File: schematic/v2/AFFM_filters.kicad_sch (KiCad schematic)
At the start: 24 parts, among them K1 DIPxx-1Axx-11x, K2 DIPxx-1Axx-11x, K3 DIPxx-1Axx-11x, K4 DIPxx-1Axx-11x

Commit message: dip switch symbol. how might this work...
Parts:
- added SW1: SW_DIP_x04, symbol Switch:SW_DIP_x04
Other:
- moved on the sheet: C12, C13, C15, C16, C17, D34, D35, D36, K2, K3, K4, R60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

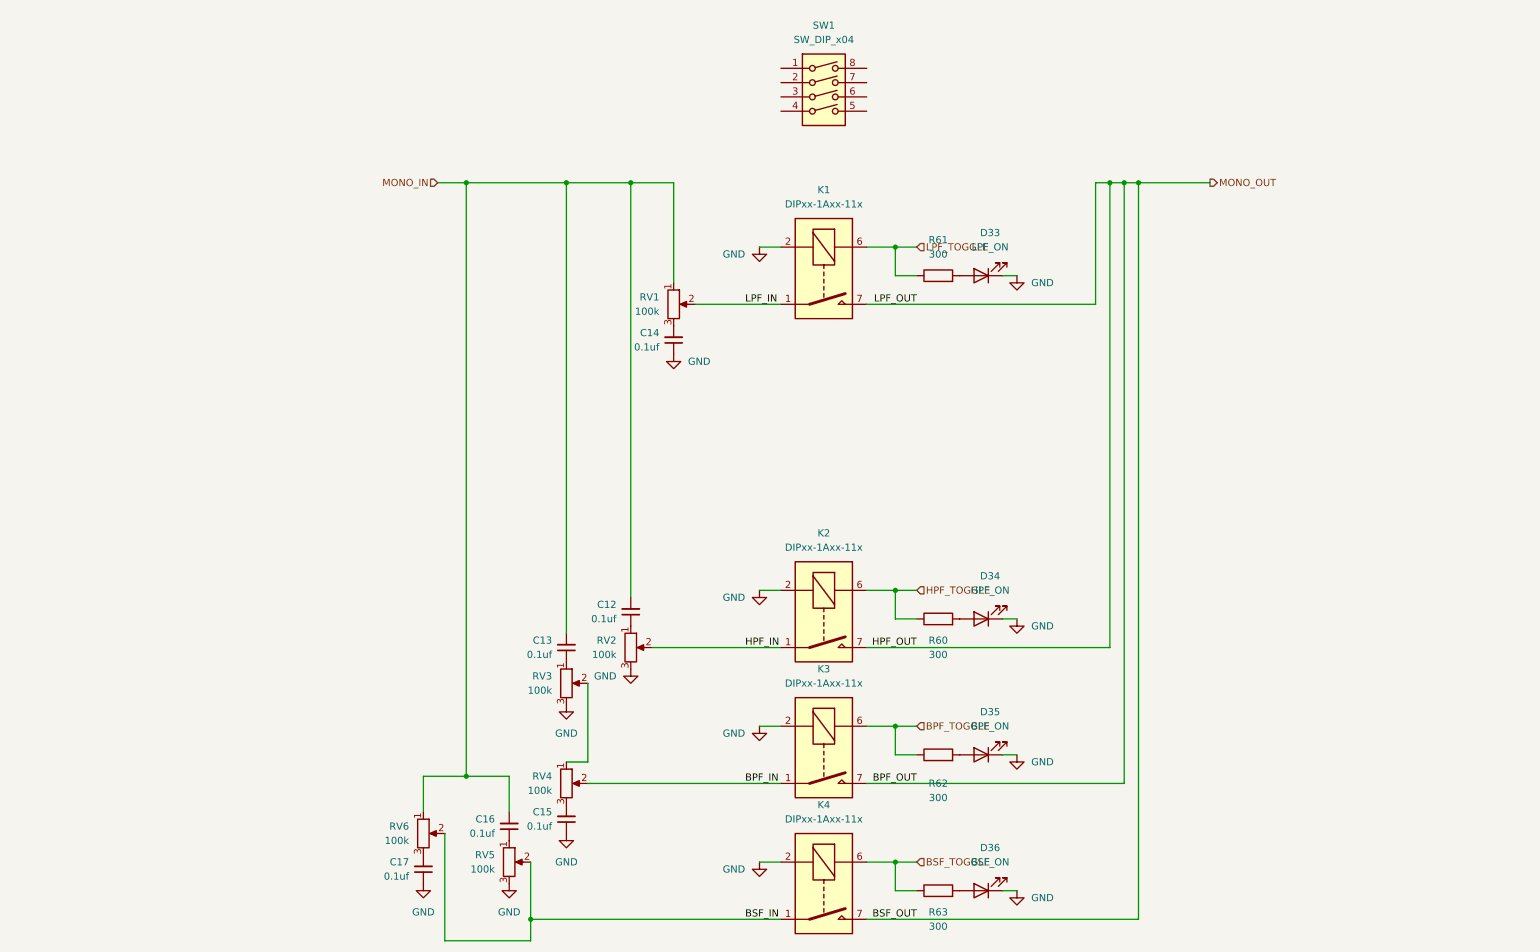
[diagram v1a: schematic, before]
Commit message: cool LPFs. i want to add some toggleability between my RC passive and active implementations...
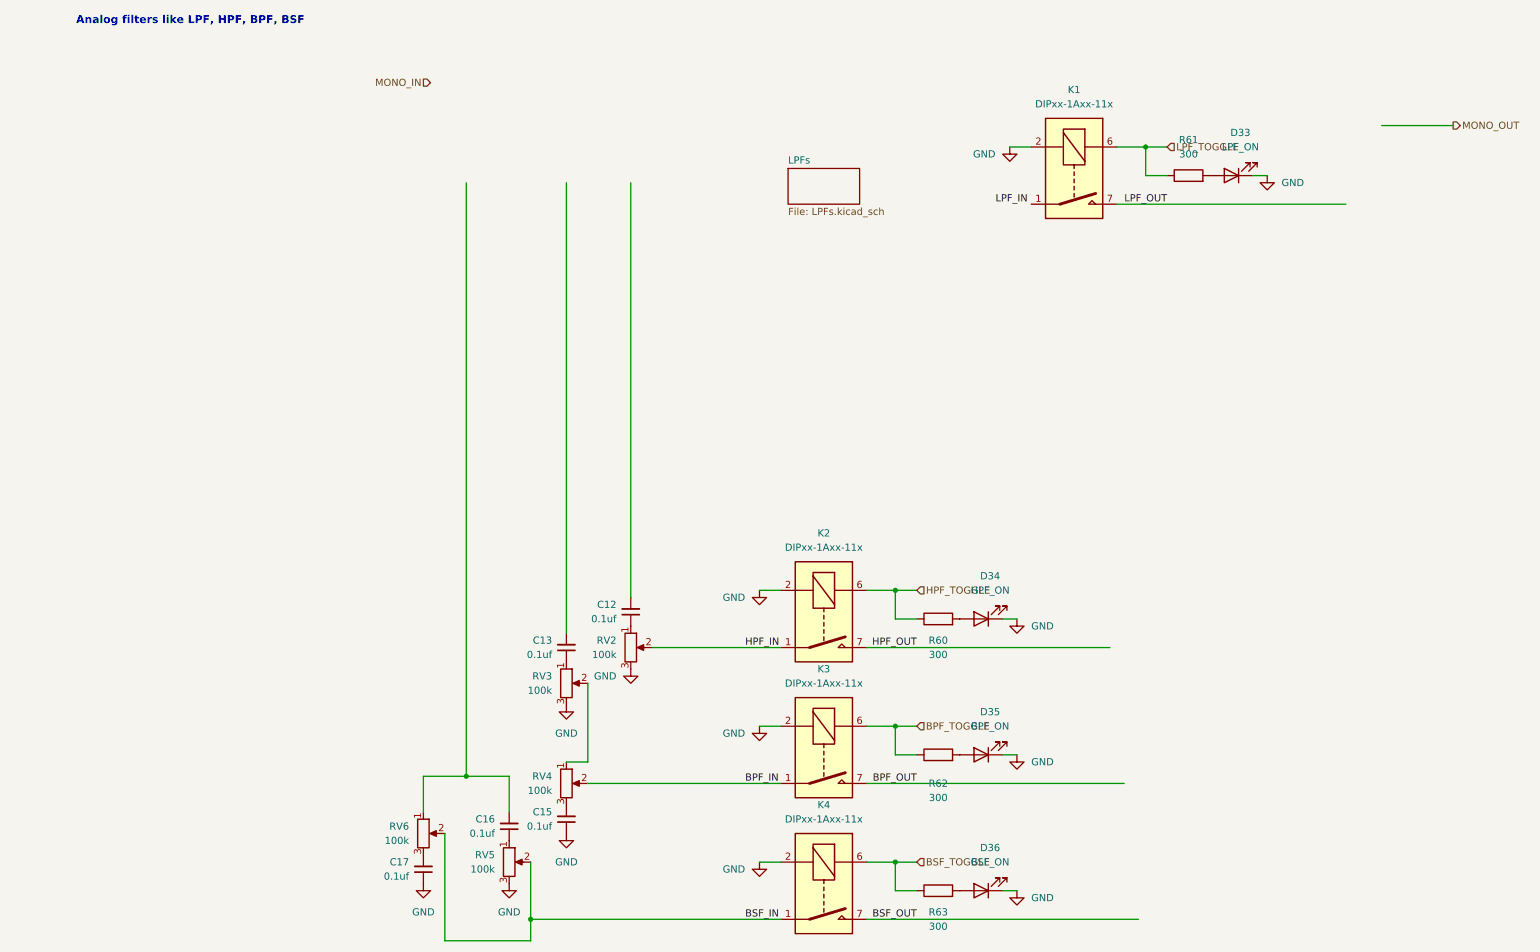
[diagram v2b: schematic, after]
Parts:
- removed C14: 0.1uf, Capacitor_SMD:C_0805_2012Metric, symbol Device:C_Small
- removed RV1: 100k, Potentiometer_THT:Potentiometer_Alps_RK09Y11_Single_Horizontal, symbol Device:R_Potentiometer
- removed SW1: SW_DIP_x04, symbol Switch:SW_DIP_x04
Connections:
- net LPF_IN: no longer K1.1, K1.14
- net MONO_IN: no longer C12.2, C13.2, C16.2, RV6.1
- net MONO_OUT: no longer K1.7, K1.8, K2.7, K2.8, K3.7, K3.8, K4.7, K4.8
- new net: C16.2, RV6.1
- new net: K1.1, K1.14
- new net BPF_OUT: K3.7, K3.8
- new net BSF_OUT: K4.7, K4.8
- new net HPF_OUT: K2.7, K2.8
- new net LPF_OUT: K1.7, K1.8
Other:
- added sheet LPFs (LPFs.kicad_sch)
- note added: "Analog filters like LPF, HPF, BPF, BSF"
- moved on the sheet: D33, K1, R61

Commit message: some progress on affm board
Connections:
- net LPF_OUT is gone; now on net MONO_OUT: K1.7, K1.8
- net LPF_IN: now also K1.1, K1.14
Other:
- sheet LPFs ports: added 12V+, 12V-, LPF_MONO_OUT, MONO_IN; removed none
- moved on the sheet: C12, C13, C15, C16, C17, D34, D35, D36, K2, K3, K4, R60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

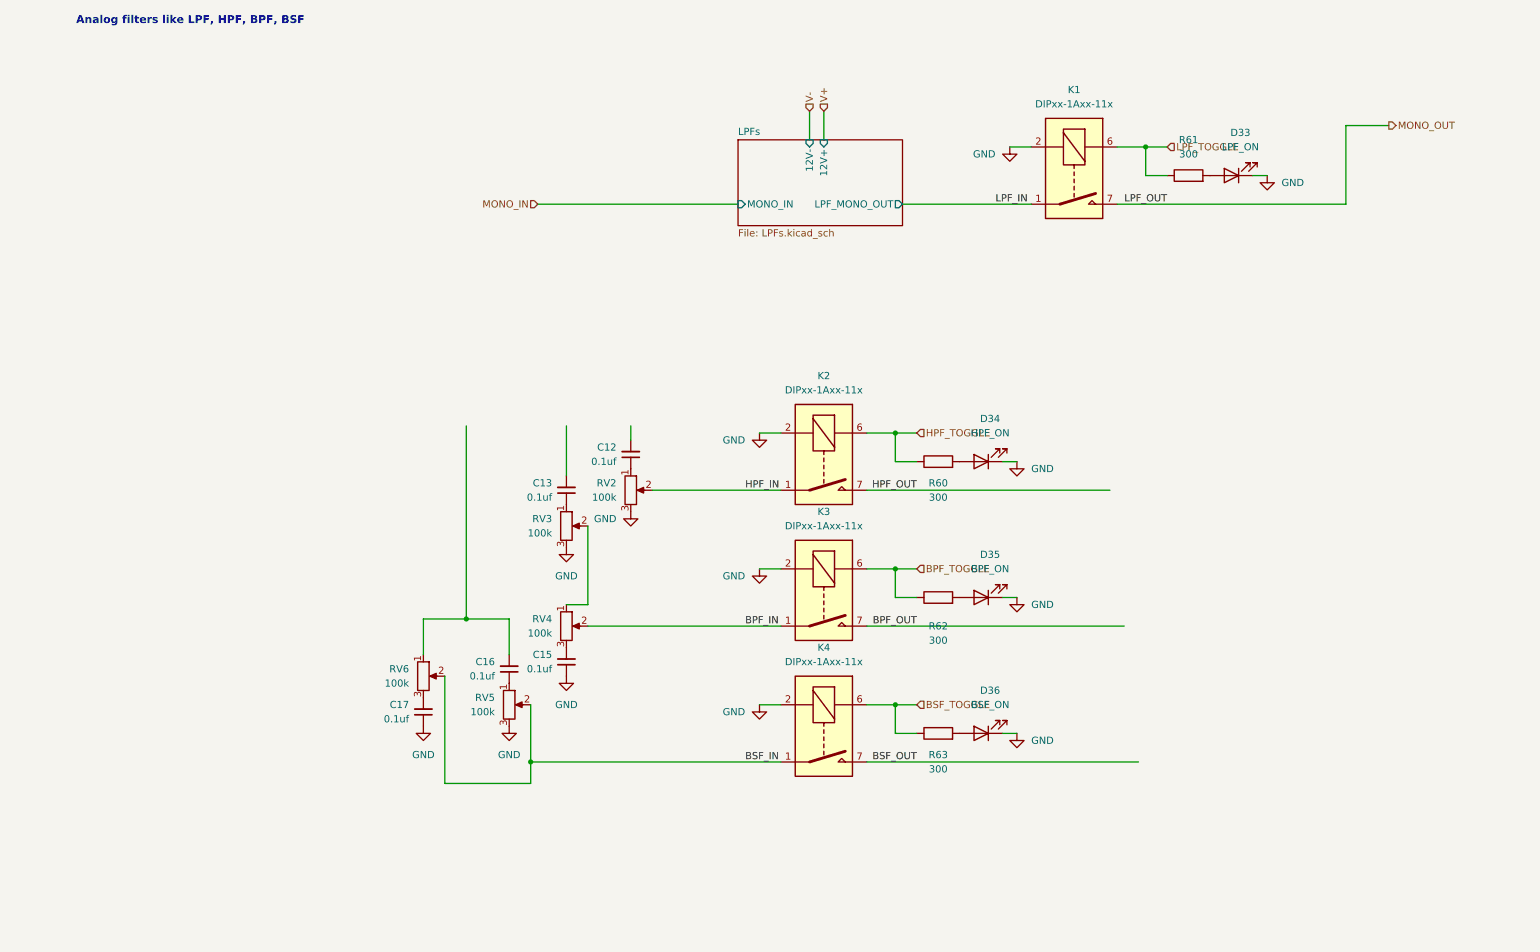
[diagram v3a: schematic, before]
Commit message: now making a v3 with HATs for each nucleo with my needed shit. this will make things very compact and hopefully much cheaper
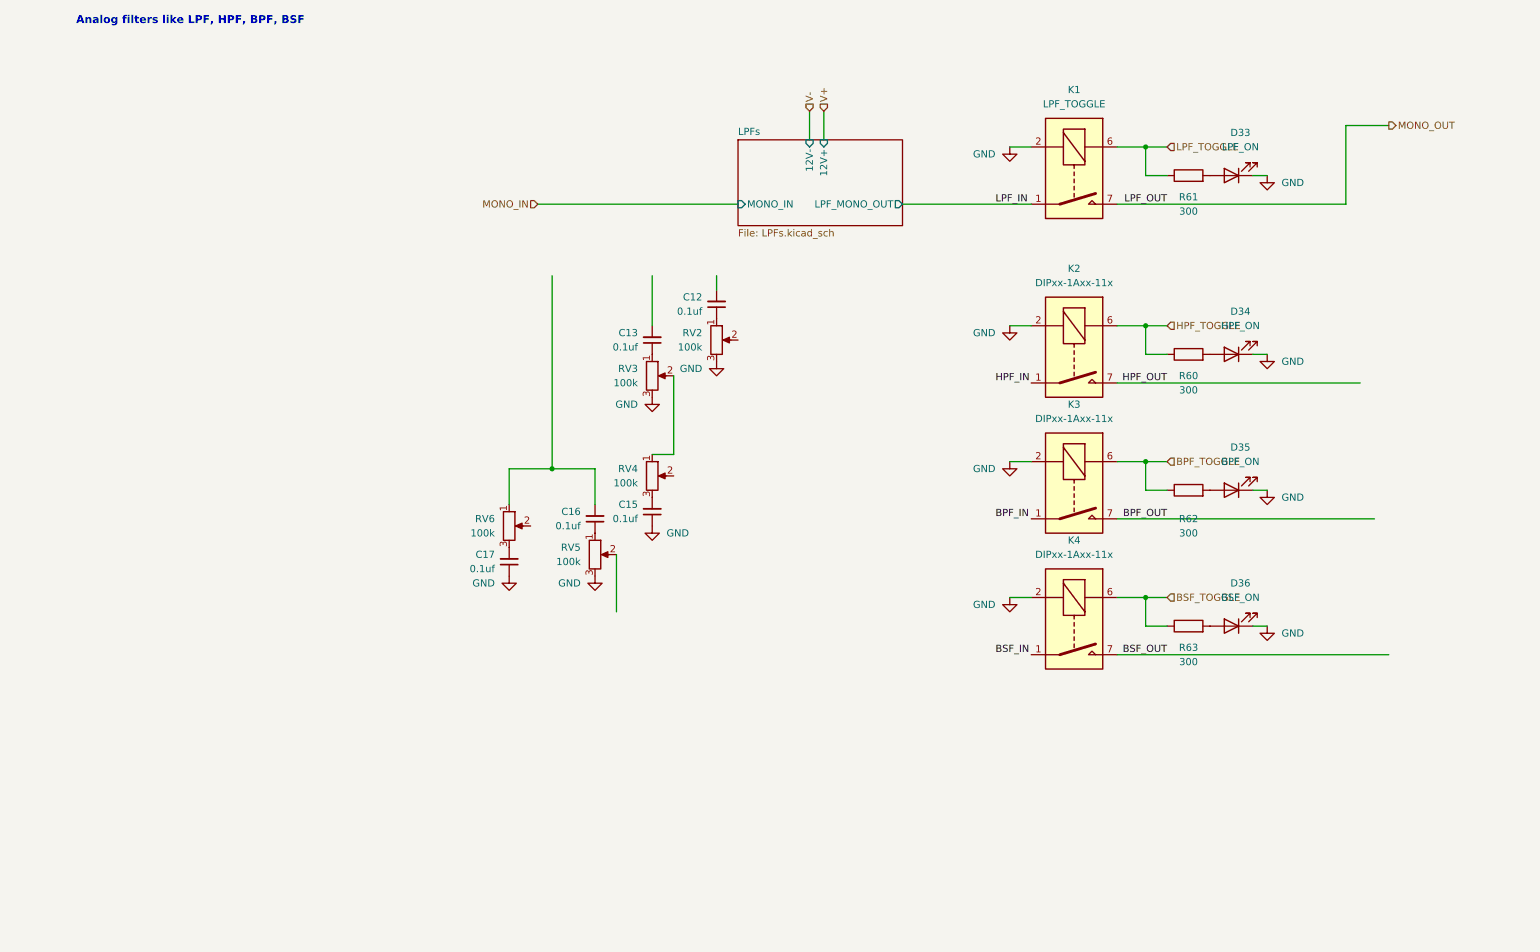
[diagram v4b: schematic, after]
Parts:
- K1: value DIPxx-1Axx-11x -> LPF_TOGGLE
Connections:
- net BPF_IN: no longer K3.1, K3.14, RV4.2
- net BSF_IN: no longer K4.1, K4.14, RV5.2, RV6.2
- net HPF_IN: no longer K2.1, K2.14, RV2.2
- new net: K3.1, K3.14
- new net: K4.1, K4.14
- new net: K2.1, K2.14
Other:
- moved on the sheet: C12, C13, C15, C16, C17, D34, D35, D36, K2, K3, K4, R60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
